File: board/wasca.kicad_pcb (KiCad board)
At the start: 2 copper layers, 100.1 x 77.4 mm, 104 parts, among them CN1 CARTRIDGE_EDGE_CONNECTOR, CN2 TFP09-2-12B, CN3 Conn_02x02_Odd_Even, CN4 Conn_02x02_Odd_Even, CN5 Conn_02x03_Odd_Even, CN6 USB-MB-S, CN7 Conn_02x05_Odd_Even, SW1 Conn_01x03_Male, U1 74ALVC164245, U10 SN74LVC1T45DBV, U11 SN74LVC1T45DBV, U12 SN74LVC1T45DBV, U13 ESP32_CAM, U2 74ALVC164245, U3 10M08SCE144I7G, U4 LD1117S33TR_SOT223, U5 74ALVC164245, U6 STM32F446RETx, U7 SDRAM_MT48_x16, U8 SN74LVC1T45DBV, U9 SN74LVC1T45DBV, Y1 Crystal

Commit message: Routing done
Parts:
- moved SW1 51.0 mm to (110.4, 122.8)
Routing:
- net /DBG_UART_RX: track 0.00 -> 42.3 mm, vias 0 -> 1
- net /LEDB: track 0.00 -> 39.8 mm, vias 0 -> 3
- net Net-(U6-Pad53): track 39.3 -> 0.00 mm
- net /LEDG: track 0.00 -> 35.9 mm, vias 0 -> 3
- net /DBG_UART_TX: track 0.00 -> 30.3 mm, vias 0 -> 2
- net /SWCLK: track 62.3 -> 55.4 mm
- net /+3_3V: track 562.5 -> 565.0 mm, vias 53 -> 54
- net Net-(SW1-Pad2): track 32.4 -> 30.0 mm
- net /+5V_USB: track 22.4 -> 24.3 mm
- net /LED3: track 27.4 -> 28.1 mm
- net /LEDR: track 35.1 -> 34.8 mm, vias 2 -> 3
- net GND: vias 194 -> 193

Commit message: Finalizing stuff for 1.4: cleanup, silkscreen, comments etc.
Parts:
- added CHAMFER_WARN1: CHAMFER_WARNING, wasca:CHAMFER_WARNING, F.Cu at (59.1, 146.2)
- added CHAMFER_WARN2: CHAMFER_WARNING, wasca:CHAMFER_WARNING, B.Cu at (77.1, 141.9)
- added R20: 5K1, Capacitor_SMD:C_0603_1608Metric_Pad1.08x0.95mm_HandSolder, F.Cu at (115.7, 95.1)
- CN6: value USB-MB-S -> USB_C_Receptacle_USB2.0; footprint wasca:con-usb-USB-MB-S -> wasca:DX07S016JA1R1500
- U13: value ESP32_CAM -> ESP32_CAM_HALF; footprint wasca:MODULE_ESP32-CAM -> wasca:MODULE_ESP32-CAM-HALF
- moved D5 19.1 mm to (52.1, 83.2)
- moved R18 18.5 mm to (54.6, 84.4), turned to 270 degrees
- moved SW1 3.81 mm to (110.4, 126.6)
- moved R7 3.03 mm to (110.2, 114.2), turned to 90 degrees
- moved CN6 2.10 mm to (124.2, 94.0), turned to 90 degrees
- moved C43 1.46 mm to (93.2, 141.2), turned to 0 degrees
- moved R2 0.76 mm to (81.9, 137.1)
- moved C21 0.64 mm to (82.0, 133.7)
- moved Y1 0.61 mm to (101.7, 119.0)
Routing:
- net /HEARTBEAT: track 59.0 -> 39.2 mm
- net Net-(CN6-PadA5): track 0.00 -> 8.72 mm
- net /+5V_USB: track 24.3 -> 32.6 mm
- net /+3_3V: track 565.0 -> 571.1 mm
- net Net-(D5-Pad1): track 7.28 -> 2.56 mm
- net /USB_DM: track 34.0 -> 30.3 mm
- net /USB_DP: track 29.0 -> 32.3 mm, vias 0 -> 2
- net Net-(SW1-Pad2): track 30.0 -> 28.0 mm
- net /ABUS_3V_CS1: track 10.4 -> 11.2 mm
- net /+5V_SATURN: track 244.4 -> 245.2 mm
- net Net-(R7-Pad1): track 12.2 -> 12.9 mm
- net GND: vias 193 -> 194

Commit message: Changing FPGA part to 10M08SCE144C8G. BOM recompilation.
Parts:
- U3: value 10M08SCE144I7G -> 10M08SCE144C8G

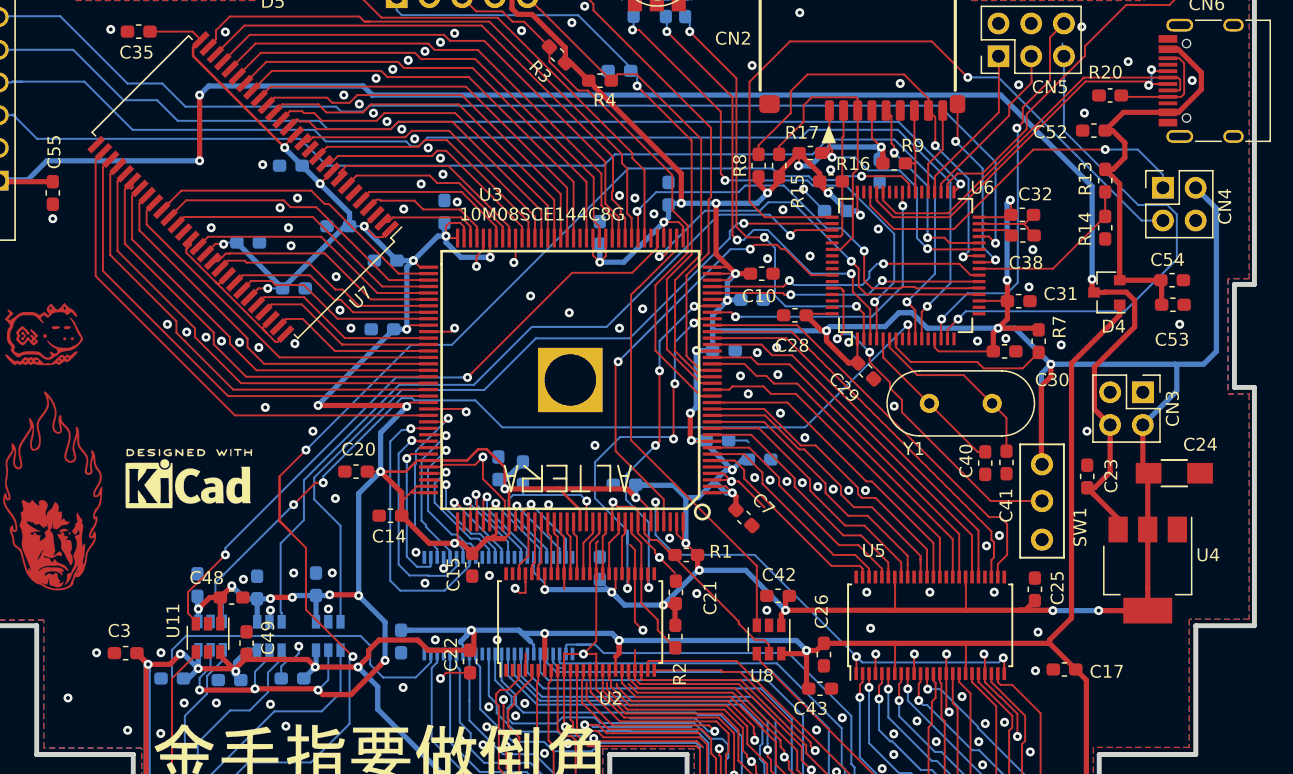
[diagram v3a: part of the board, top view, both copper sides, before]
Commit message: SSEL pin duplicated to STM32
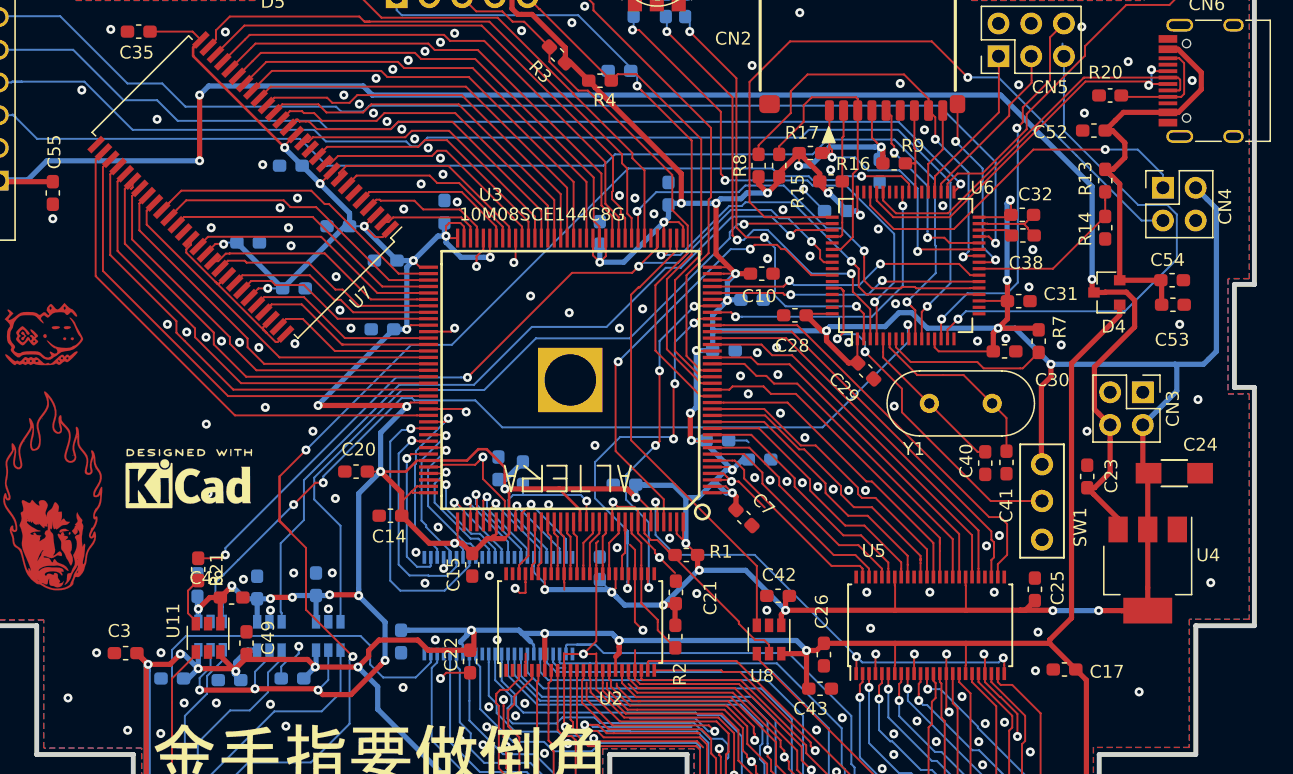
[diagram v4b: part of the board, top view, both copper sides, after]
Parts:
- added R21: 0, Capacitor_SMD:C_0603_1608Metric_Pad1.08x0.95mm_HandSolder, F.Cu at (44.9, 131.9)
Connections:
- U11 pad 3: /SSEL_3V -> Net-(R21-Pad2)
- U6 pad 56: Net-(U6-Pad56) -> /SSEL_3V
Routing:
- net /SSEL_3V: track 51.3 -> 65.6 mm, vias 2 -> 4
- net /+3_3V: track 571.1 -> 566.8 mm
- net Net-(R21-Pad2): track 0.00 -> 3.93 mm
- net /ISD_3V: track 68.7 -> 69.5 mm
- net /SD_DAT2: track 21.8 -> 22.5 mm
- net GND: vias 194 -> 206

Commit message: PCB production preparement
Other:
- board text added: "Mfg. date : 2020 December 19"
- board text removed: "Mfg. date : 2020 December ??"
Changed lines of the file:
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@@
   (general
     (thickness 1.6002)
-    (drawings 55)
+    (drawings 58)
     (tracks 2890)
     (zones 0)
@@
     (visible_elements 7FFFFFFF)
     (pcbplotparams
-      (layerselection 0x020f0_80000001)
+      (layerselection 0x010f0_ffffffff)
       (usegerberextensions true)
       (usegerberattributes true)
@@
       (plotinvisibletext false)
       (padsonsilk false)
-      (subtractmaskfromsilk false)
+      (subtractmaskfromsilk true)
       (outputformat 1)
       (mirror false)
@@
       (effects (font (size 1 1) (thickness 0.15)))
     )
-    (fp_text user %R (at 0 0 90) (layer F.Fab)
-      (effects (font (size 0.4 0.4) (thickness 0.06)))
-    )
     (fp_line (start -0.8 0.4) (end -0.8 -0.4) (layer F.Fab) (width 0.1))
     (fp_line (start -0.8 -0.4) (end 0.8 -0.4) (layer F.Fab) (width 0.1))
@@
     (fp_line (start 1.65 -0.73) (end 1.65 0.73) (layer F.CrtYd) (width 0.05))
     (fp_line (start 1.65 0.73) (end -1.65 0.73) (layer F.CrtYd) (width 0.05))
+    (fp_text user %R (at 0 0 90) (layer F.Fab)
+      (effects (font (size 0.4 0.4) (thickness 0.06)))
+    )
     (pad 2 smd roundrect (at 0.8625 0 270) (size 1.075 0.95) (layers Front F.Paste F.Mask) (roundrect_rratio 0.25)
       (net 269 "Net-(R21-Pad2)"))
@@
     )
   )
+  (dimension 45.851659 (width 0.381) (layer Dwgs.User)
+    (gr_text "45,852 мм" (at 44.471175 62.303948 25.01689348) (layer Dwgs.User)
+      (effects (font (size 1 1) (thickness 0.15)))
+    )
+    (feature1 (pts (xy 68.56 59.71) (xy 65.645624 53.46491)))
+    (feature2 (pts (xy 27.01 79.1) (xy 24.095624 72.85491)))
+    (crossbar (pts (xy 24.343613 73.386314) (xy 65.893613 53.996314)))
+    (arrow1a (pts (xy 65.893613 53.996314) (xy 65.120783 55.004101)))
+    (arrow1b (pts (xy 65.893613 53.996314) (xy 64.624805 53.941291)))
+    (arrow2a (pts (xy 24.343613 73.386314) (xy 25.612421 73.441337)))
+    (arrow2b (pts (xy 24.343613 73.386314) (xy 25.116443 72.378527)))
+  )
+  (dimension 0.172627 (width 0.381) (layer Dwgs.User)
+    (gr_text "0,173 мм" (at 25.557296 79.708935 79.9920202) (layer Dwgs.User)
+      (effects (font (size 1 1) (thickness 0.15)))
+    )
+    (feature1 (pts (xy 27.05 80.06) (xy 26.472502 79.958089)))
+    (feature2 (pts (xy 27.08 79.89) (xy 26.502502 79.788089)))
+    (crossbar (pts (xy 27.08 79.89) (xy 27.05 80.06)))
+    (arrow1a (pts (xy 27.05 80.06) (xy 26.668272 78.848726)))
+    (arrow1b (pts (xy 27.05 80.06) (xy 27.823267 79.052549)))
+    (arrow2a (pts (xy 27.08 79.89) (xy 26.306733 80.897451)))
+    (arrow2b (pts (xy 27.08 79.89) (xy 27.461728 81.101274)))
+  )
+  (dimension 100.120084 (width 0.381) (layer Dwgs.User)
+    (gr_text "100,120 мм" (at 76.972196 79.513859 359.9256048) (layer Dwgs.User)
+      (effects (font (size 1 1) (thickness 0.15)))
+    )
+    (feature1 (pts (xy 127.03 81.27) (xy 127.030969 80.523438)))
+    (feature2 (pts (xy 26.91 81.14) (xy 26.910969 80.393438)))
+    (crossbar (pts (xy 26.910208 80.979858) (xy 127.030208 81.109858)))
+    (arrow1a (pts (xy 127.030208 81.109858) (xy 125.902944 81.694816)))
+    (arrow1b (pts (xy 127.030208 81.109858) (xy 125.904467 80.521975)))
+    (arrow2a (pts (xy 26.910208 80.979858) (xy 28.035949 81.567741)))
+    (arrow2b (pts (xy 26.910208 80.979858) (xy 28.037472 80.3949)))
+  )
   (gr_line (start 52.375 120.255) (end 28.2 120.255) (angle 90) (layer B.SilkS) (width 0.381))
   (gr_line (start 52.375 122.555) (end 52.375 120.255) (angle 90) (layer B.SilkS) (width 0.381))
@@
   (gr_line (start 33.68 98.71) (end 56.705 98.71) (angle 90) (layer B.SilkS) (width 0.381))
   (gr_line (start 33.68 90.81) (end 33.68 98.71) (angle 90) (layer B.SilkS) (width 0.381))
-  (gr_text "Mfg. date : 2020 December ??" (at 40.8 121.38) (layer B.SilkS)
+  (gr_text "Mfg. date : 2020 December 19" (at 40.8 121.38) (layer B.SilkS)
     (effects (font (size 0.8992 0.8992) (thickness 0.1905)) (justify mirror))
   )

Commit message: Board 1.5 update (unchecked)
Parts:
- added R22: 0, Capacitor_SMD:C_0603_1608Metric_Pad1.08x0.95mm_HandSolder, B.Cu at (98.0, 83.2)
- added R23: 0, Capacitor_SMD:C_0603_1608Metric_Pad1.08x0.95mm_HandSolder, B.Cu at (74.4, 87.1)
- added R24: 470, Capacitor_SMD:C_0603_1608Metric_Pad1.08x0.95mm_HandSolder, F.Cu at (112.6, 112.2)
- CHAMFER_WARN1, CHAMFER_WARN2: value CHAMFER_WARNING -> LOGO
- moved U1 0.20 mm to (68.2, 134.5)
- moved U2 0.18 mm to (74.6, 135.8)
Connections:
- CN5 pad 1: /SPARE2 -> /JTAG_TCK
- CN5 pad 3: /SPARE1 -> /JTAG_TMS
- U1 pad 25: GND -> /BUFFERS_OE
- U1 pad 48: GND -> /BUFFERS_OE
- U2 pad 2: Net-(U2-Pad2) -> GND
- U2 pad 25: GND -> /BUFFERS_OE
- U2 pad 48: GND -> /BUFFERS_OE
- U5 pad 25: GND -> /BUFFERS_OE
- U5 pad 48: GND -> /BUFFERS_OE
- U6 pad 16: Net-(U6-Pad16) -> /BUFFERS_OE
- U6 pad 17: Net-(U6-Pad17) -> /5V_SATURN_DETECT
- U6 pad 35: /SPARE1 -> /JTAG_TMS
- U6 pad 36: /SPARE2 -> /JTAG_TCK
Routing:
- net /BUFFERS_OE: track 0.00 -> 89.6 mm, vias 0 -> 9
- net /JTAG_TMS: track 43.8 -> 109.5 mm
- net /JTAG_TDO: track 54.0 -> 96.4 mm
- net /DBG_UART_TX: track 30.3 -> 71.9 mm, vias 2 -> 3
- net /JTAG_TCK: track 50.3 -> 91.3 mm
- net /DBG_UART_RX: track 42.3 -> 64.0 mm
- net /SPARE1: track 13.4 -> 0.00 mm
- net /SPARE2: track 12.6 -> 0.00 mm
- net /5V_SATURN_DETECT: track 0.00 -> 6.38 mm, vias 0 -> 2
- net GND: track 437.0 -> 431.4 mm, vias 206 -> 207
- net /JTAG_TDI: track 39.5 -> 42.7 mm
- net /ABUS_CS0: track 33.7 -> 35.6 mm
- net /+3_3V: track 566.8 -> 568.3 mm
- net /ISD_3V: track 69.5 -> 71.0 mm
- net Net-(SW1-Pad2): track 28.3 -> 27.1 mm
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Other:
- board text added: "Mfg. date : 2021 July ??"
- board text added: "wasca v. 1.5 By hitomi2500 & cafe-alpha http://ppcenter.free.fr/satcart/ http://wasca.info/"
- board text removed: "Mfg. date : 2020 December 19"
- board text removed: "wasca v. 1.4 By hitomi2500 & cafe-alpha http://ppcenter.free.fr/satcart/ http://wasca.info/"

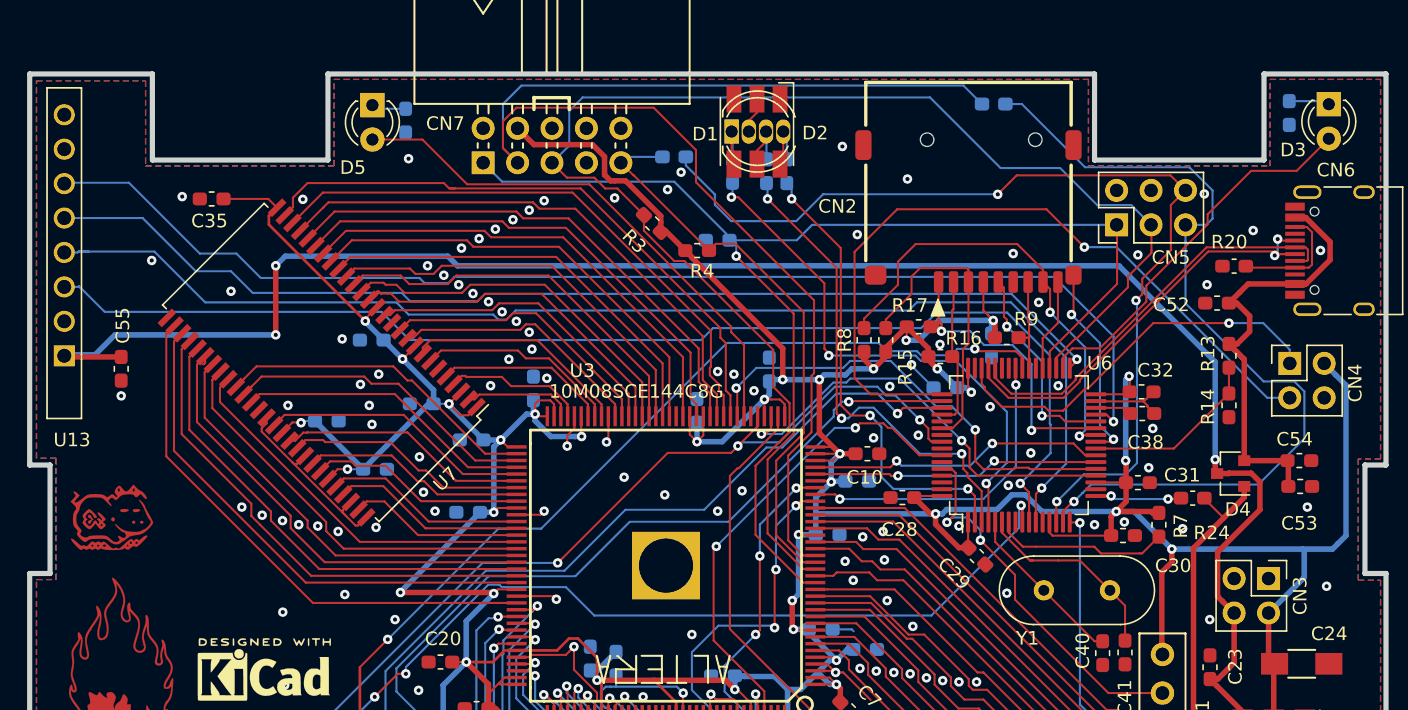
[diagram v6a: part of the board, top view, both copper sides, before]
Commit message: Board 1.5 , STM-to-MAX JTAG detached from UART
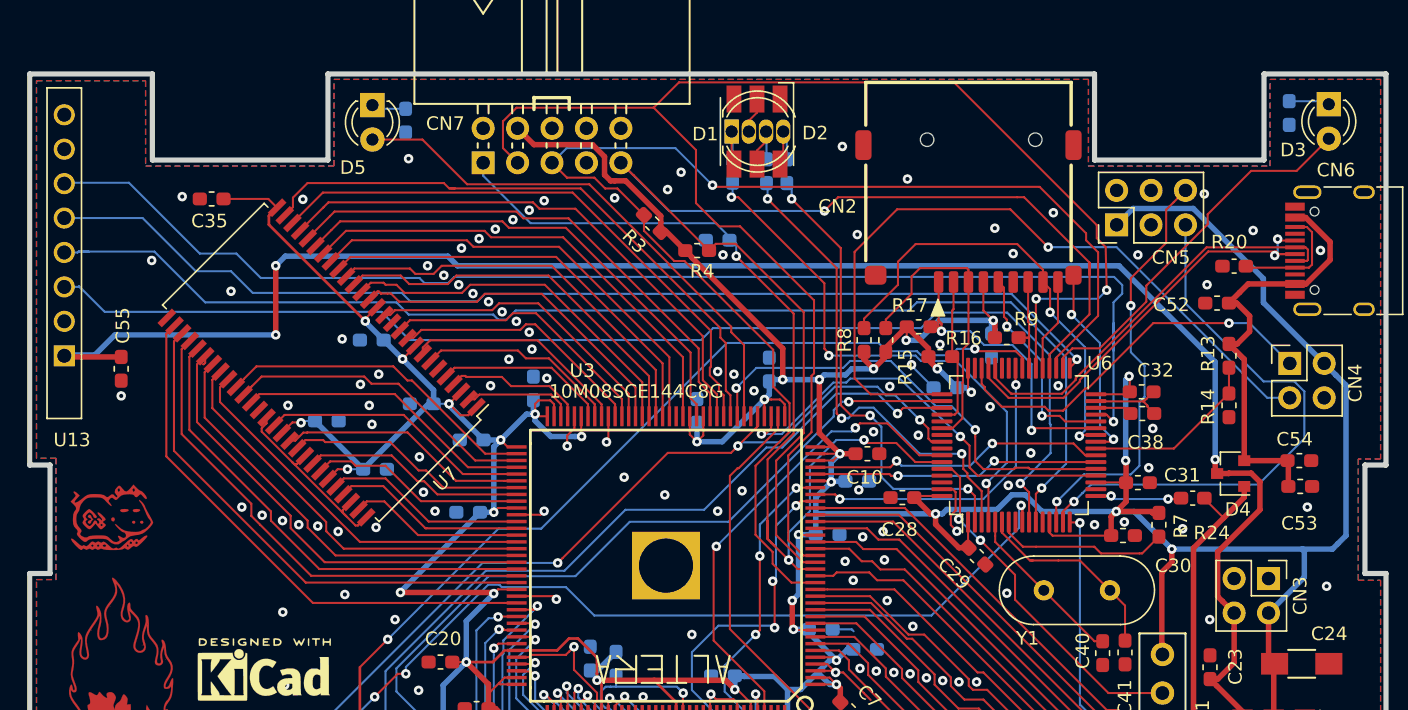
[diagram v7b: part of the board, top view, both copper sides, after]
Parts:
- removed R22, R23: 0, Capacitor_SMD:C_0603_1608Metric_Pad1.08x0.95mm_HandSolder
- CHAMFER_WARN1, CHAMFER_WARN2: value LOGO -> CHAMFER_WARNING
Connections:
- CN5 pad 1: /JTAG_TCK -> /+3_3V
- CN5 pad 3: /JTAG_TMS -> Net-(CN5-Pad3)
- U6 pad 36: /JTAG_TCK -> /JTAG_TDI
- U6 pad 38: Net-(U6-Pad38) -> /JTAG_TDO
- U6 pad 59: Net-(U6-Pad59) -> /JTAG_TCK
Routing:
- net /JTAG_TDI: track 42.7 -> 87.8 mm, vias 0 -> 1
- net /DBG_UART_TX: track 71.9 -> 31.3 mm, vias 3 -> 2
- net /DBG_UART_RX: track 64.0 -> 41.8 mm
- net /+3_3V: track 568.3 -> 589.9 mm
- net /JTAG_TCK: track 91.3 -> 71.9 mm, vias 1 -> 3
- net /JTAG_TDO: track 96.4 -> 109.5 mm, vias 0 -> 2
- net /JTAG_TMS: track 109.5 -> 99.0 mm, vias 0 -> 1
- net GND: track 431.4 -> 436.7 mm, vias 207 -> 210
- net /ESP32_SCK: track 90.3 -> 95.4 mm
- net Net-(SW1-Pad2): track 27.1 -> 25.3 mm
- net /SWDIO: track 29.4 -> 28.8 mm
